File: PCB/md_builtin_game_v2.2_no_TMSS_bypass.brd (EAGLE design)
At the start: 81.3 x 36.8 mm, 18 parts, among them IC1 MX29F1610A, IC2 ATF16V8BS

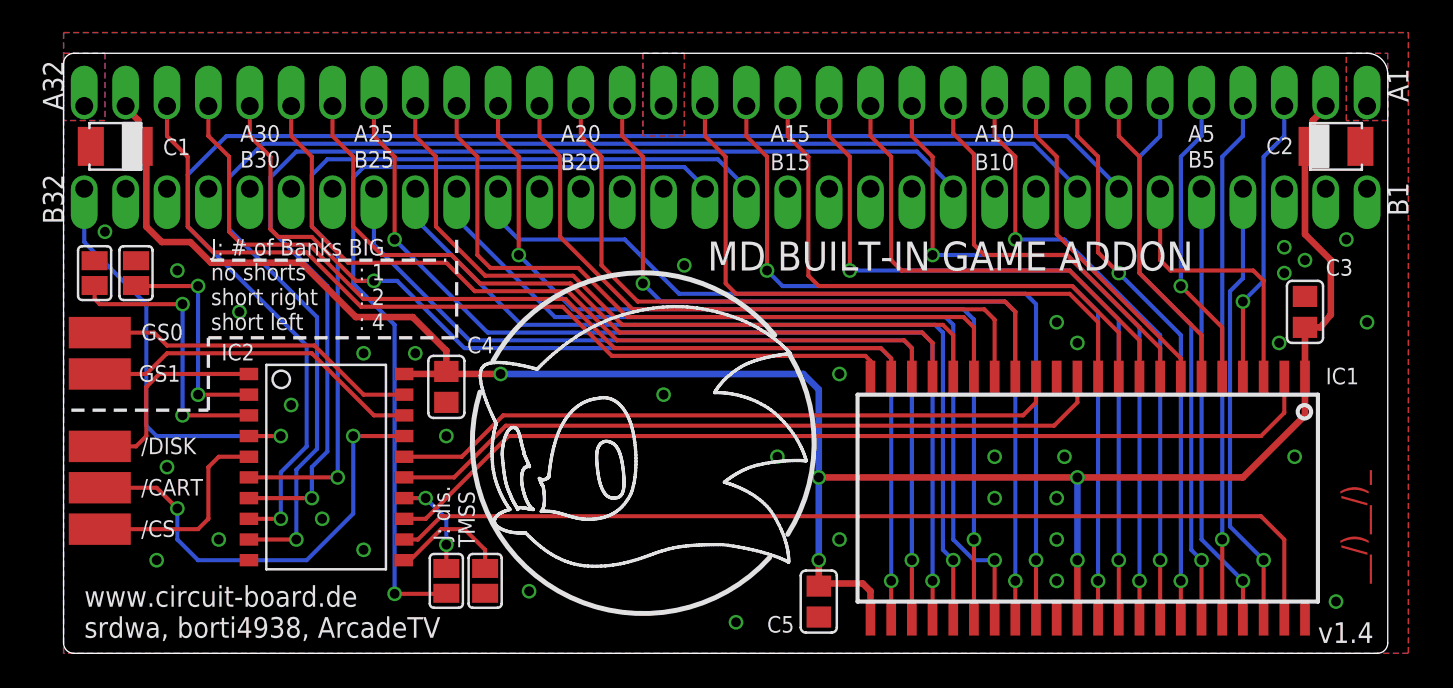
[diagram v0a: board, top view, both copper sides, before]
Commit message: Update PCB Version from v1.4 to v2.x - v2.1 has an optional (switchable) TMSS bypass mod included (TMSS bypass is enabled if /M30 (cart slot B30) is high and if the jumpers are set to on or to switchable with the pad ‚TS’ set to high) - v2.2 has no TMSS bypass mod included - v2.3 has the TMSS bypass mod included (TMSS bypass is enabled if /M30 (cart slot B30) is high) For all PCB versions, the PLD code v2.0 is to use.
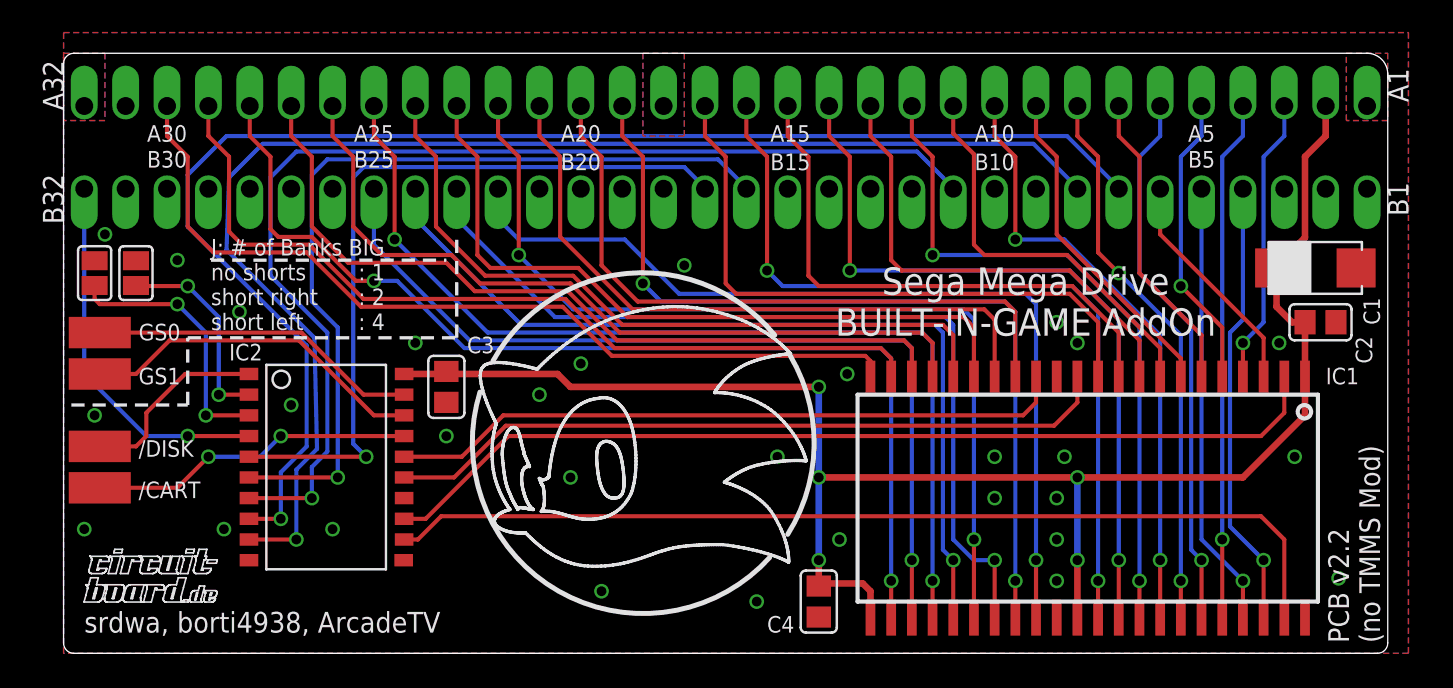
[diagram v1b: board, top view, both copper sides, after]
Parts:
- removed C5: 100nF, arcadetv:Z0805
- removed SJ3, SJ4: (no value), jumper:SJ
- removed U$2: /CS_K, arcadetv:PADS
- removed U$3: /CART_K, arcadetv:PADS
- removed U$4: /DISK (ExpPort B2), arcadetv:PADS
- removed U$5: BIG_Sel0, arcadetv:PADS
- removed U$7: BIG_Sel_1, arcadetv:PADS
- added /CART, /DISK, GS0, GS1: PAD, snes_div:PADS
- C1: value 22uF/6.3V -> 22uF; device rcl:SMC_B -> rcl:SMC_C
- C2: value 22uF -> 100nF; device rcl:SMC_B -> arcadetv:Z0805
- moved C1 74.0 mm to (76.8, 23.7), turned to 0 degrees
- moved C3 52.9 mm to (23.5, 16.4), turned to 90 degrees
- moved C4 26.4 mm to (46.4, 3.17)
- moved C2 10.8 mm to (77.2, 20.3), turned to 180 degrees
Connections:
- net /CHECK renamed CART_/CART
- removed net +5V: C1.+, C2.+, C3.2, C4.2, C5.2, IC1.1, IC1.23, IC1.33, IC2.20, U$6.A2, U$6.A31
- removed net ASIC_/CS: IC2.5, U$2.P$1
- removed net CART_/CS: SJ4.2, U$6.B17
- removed net TMSS_MOD: IC2.11, SJ3.1
- new net CART_/OE: IC2.5, U$6.B17
- new net VCC: C1.+, C2.2, C3.2, C4.2, IC1.1, IC1.23, IC1.33, IC2.20, U$6.A2
- net /DISK: now also /DISK.P$1; no longer U$4.P$1
- net ASIC_/CART: now also /CART.P$1; no longer U$3.P$1
- net BIG_SEL0: now also GS0.P$1; no longer U$5.P$1
- net BIG_SEL1: now also GS1.P$1; no longer U$7.P$1
- net GND: now also C2.1, IC2.11; no longer C2.-, C5.1, SJ3.2
- net N$1: no longer SJ4.1
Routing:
- net +5V: track 135.8 -> 0.00 mm, vias 5 -> 0
- net VCC: track 0.00 -> 105.3 mm, vias 0 -> 5
- net CART_/CS: track 52.2 -> 0.00 mm, vias 1 -> 0
- net CART_/OE: track 0.00 -> 47.1 mm, vias 0 -> 1
- net ASIC_/CS: track 12.9 -> 0.00 mm
- net ASIC_/CART: track 27.6 -> 20.0 mm
- net TMSS_MOD: track 7.46 -> 0.00 mm
- net N$1: track 6.16 -> 0.00 mm, vias 2 -> 0
- net CART_/CART: track 26.6 -> 23.1 mm
- net A18: track 17.3 -> 14.3 mm
- net BIG_SEL1: track 20.8 -> 23.0 mm
- net MODE2: track 14.9 -> 13.8 mm
- net MODE4: track 17.3 -> 16.2 mm
- net /DISK: track 12.8 -> 11.8 mm
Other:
- board text added: ": MX29F1610 : ATF16V8B : 22uF (6.3V+) : 100nF (50V)"
- board text added: "IC1 IC2 C1 C2-C4"
- board text added: "PCB v2.2 (no TMMS Mod)"
- board text added: "Sega Mega Drive BUILT-IN-GAME AddOn"
- board text added: "[44 SOP (500mil)] [20SOIC] [Tantal SMD-C] [SMD 0805]"
- board text added: "srdwa, borti4938, ArcadeTV"
- board text removed: ")"
- board text removed: "/"
- board text removed: "/CS"
- board text removed: "J: dis. TMSS"
- board text removed: "MD BUILT-IN GAME ADDON"
- board text removed: "_"
- board text removed: "__/)__/)_"
- board text removed: "v1.4"
- board text removed: "www.circuit-board.de srdwa, borti4938, ArcadeTV"
